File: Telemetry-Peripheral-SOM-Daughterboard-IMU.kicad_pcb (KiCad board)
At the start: 2 copper layers, 39 x 54 mm, 34 parts, among them IC1 FS3000-1015, J1 Conn_02x10_Odd_Even, J2 Conn_01x03_Pin, J3 Conn_01x03_Pin, J4 Conn_01x03_Pin, U1 LSM6DSV

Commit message: changes to I2C
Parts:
- renumbered Temp1 to TP1, Temp2 to TP2, Temp3 to TP3, Airflow_SDA to TP4, Airflow_SCL to TP5
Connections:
- IC1 pad 6: /I2C2_SDA -> /I2C1_SDA
- IC1 pad 7: /I2C2_SCL -> /I2C1_SCL
- TP4 pad 1: /I2C2_SDA -> /I2C1_SDA
- TP5 pad 1: /I2C2_SCL -> /I2C1_SCL
- U1 pad 4: /I2C1_SDA -> /I2C2_SDA
- U1 pad 9: /I2C1_SCL -> /I2C2_SCL
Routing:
- net /I2C2_SCL: track 43.3 -> 18.5 mm, vias 3 -> 0
- net /I2C1_SCL: track 17.5 -> 41.6 mm, vias 2 -> 1
- net /I2C2_SDA: track 44.4 -> 22.3 mm, vias 3 -> 2
- net /I2C1_SDA: track 22.7 -> 38.2 mm

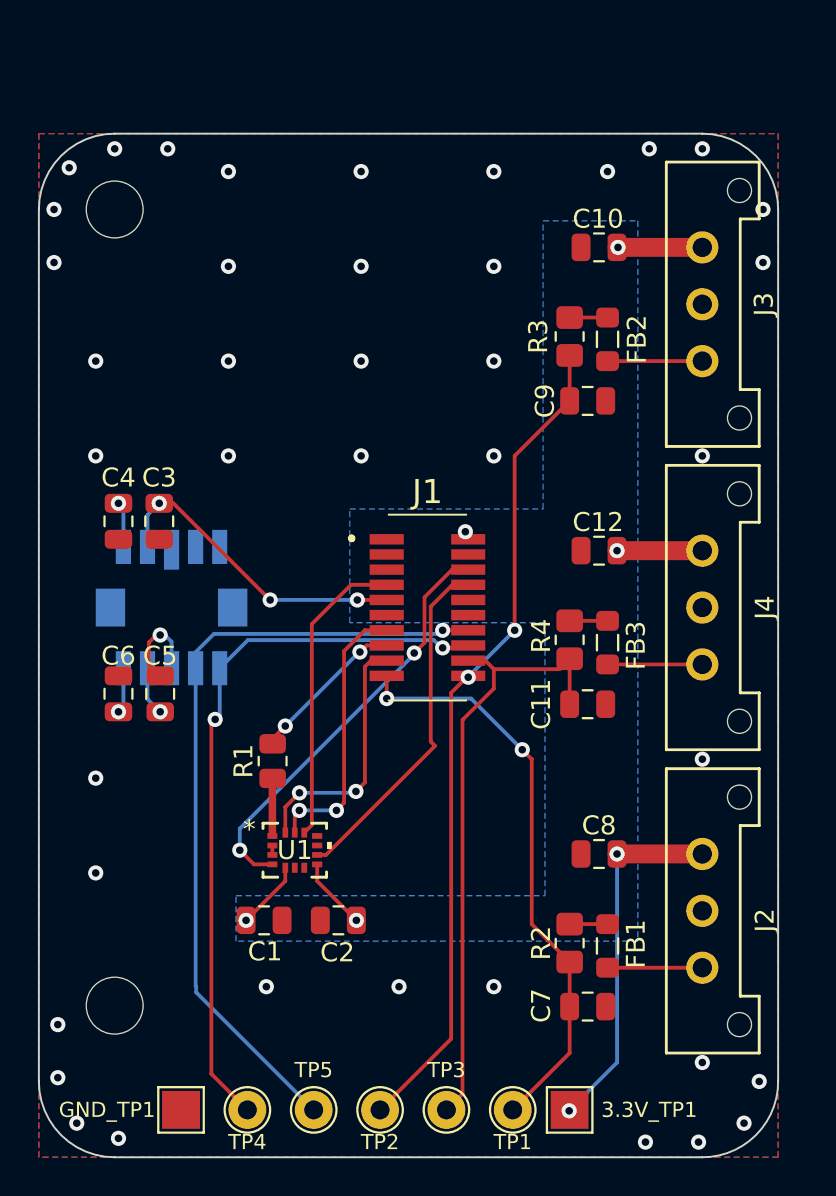
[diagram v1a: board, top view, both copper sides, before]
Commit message: moved testPoints to top of board
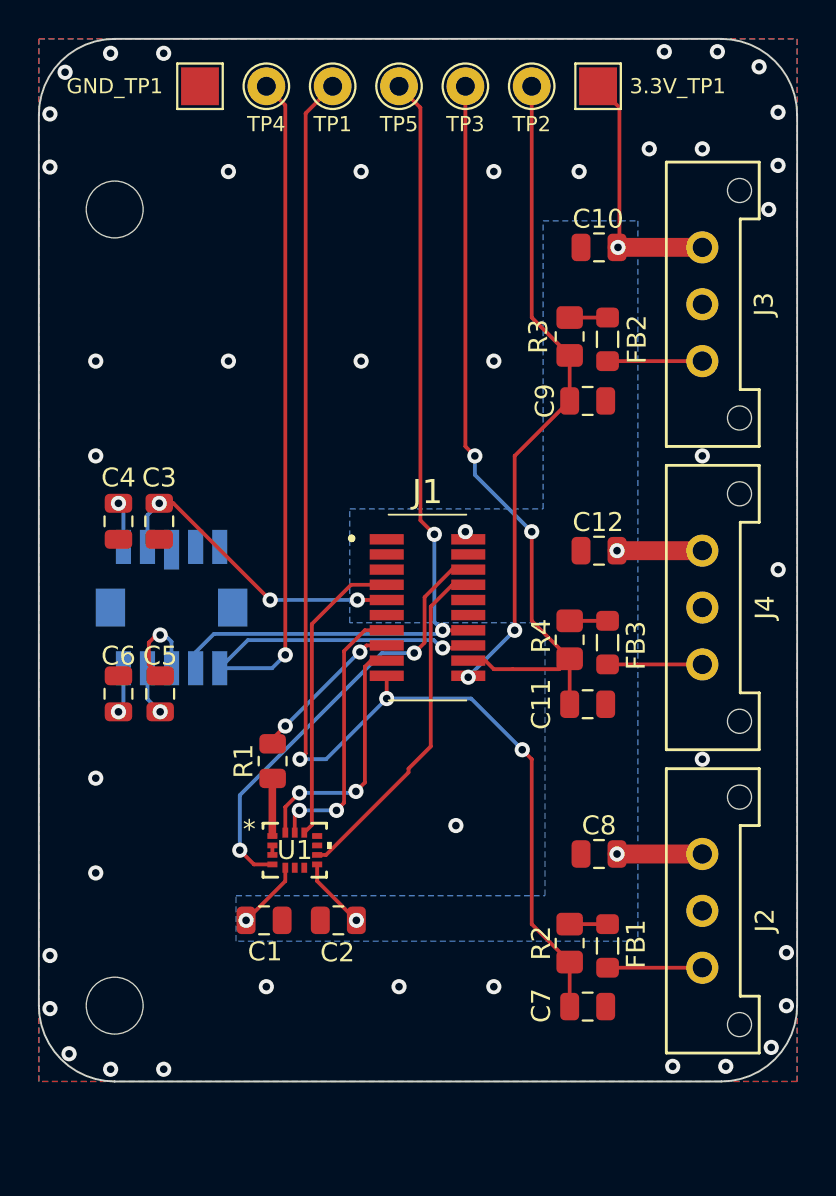
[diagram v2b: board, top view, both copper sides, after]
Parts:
- moved TP1 54.8 mm to (161.5, 63.5)
- moved TP2 54.6 mm to (172.0, 63.5)
- moved TP5 54.2 mm to (165.0, 63.5)
- moved 3.3V_TP1 54.0 mm to (175.5, 63.5)
- moved GND_TP1 54.0 mm to (154.5, 63.5)
- moved TP3 54.0 mm to (168.5, 63.5)
- moved TP4 54.0 mm to (158.0, 63.5)
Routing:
- net /SPI1_NSS: track 30.7 -> 66.2 mm, vias 2 -> 3
- net /I2C1_SDA: track 38.2 -> 48.1 mm
- net /PA1: track 44.0 -> 34.2 mm
- net /PA2: track 32.4 -> 40.6 mm, vias 0 -> 2
- net +3.3V: track 52.8 -> 47.1 mm, vias 10 -> 9
- net /I2C1_SCL: track 41.6 -> 45.4 mm, vias 1 -> 2
- net /I2C2_SDA: track 22.3 -> 23.4 mm
- net GND: vias 40 -> 41
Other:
- board size 39 x 54 mm -> 40 x 55 mm

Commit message: changes to silkscreen naming
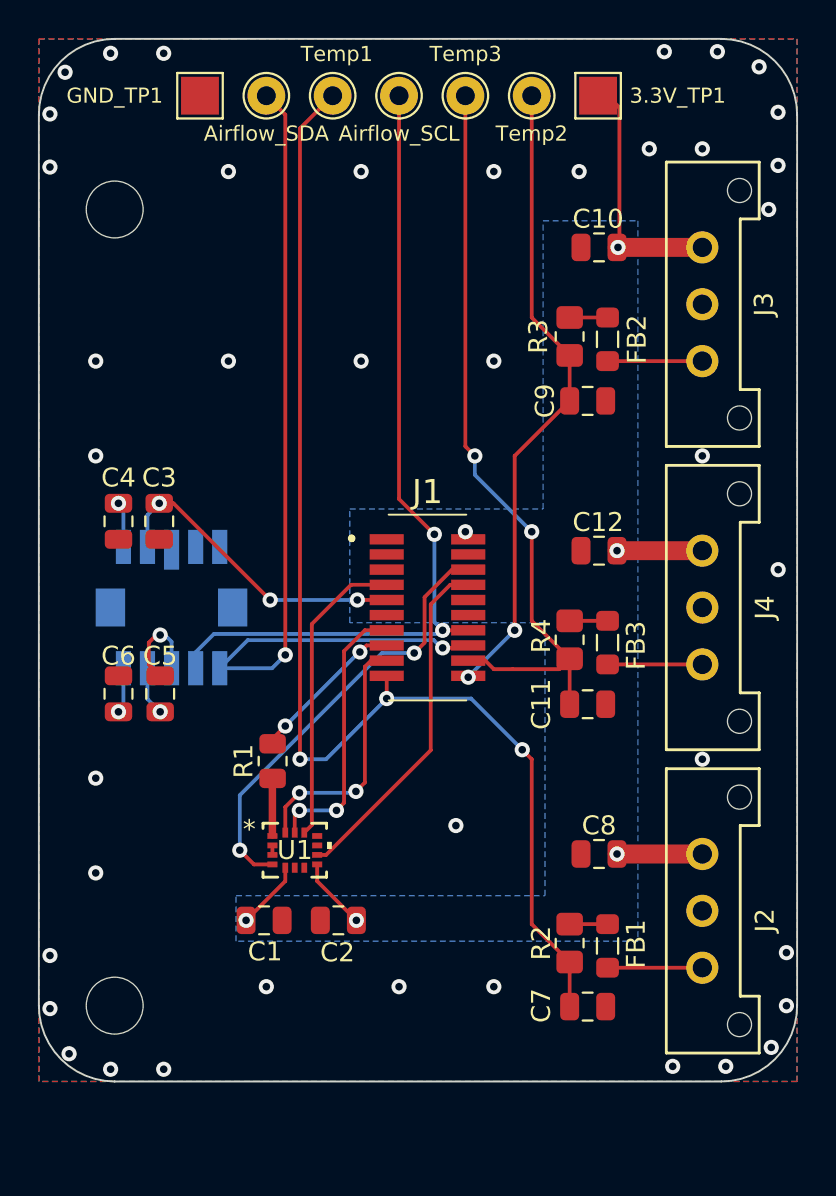
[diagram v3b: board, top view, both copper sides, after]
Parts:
- moved 3.3V_TP1 0.50 mm to (175.5, 64.0)
- moved Airflow_SCL 0.50 mm to (165.0, 64.0)
- moved Airflow_SDA 0.50 mm to (158.0, 64.0)
- moved GND_TP1 0.50 mm to (154.5, 64.0)
- moved Temp1 0.50 mm to (161.5, 64.0)
- moved Temp2 0.50 mm to (172.0, 64.0)
- moved Temp3 0.50 mm to (168.5, 64.0)
- renumbered TP5 to Airflow_SCL, TP4 to Airflow_SDA, TP1 to Temp1, TP2 to Temp2, TP3 to Temp3
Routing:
- net /SPI1_NSS: track 66.2 -> 65.7 mm
- net /PA2: track 40.6 -> 40.1 mm
- net /PA1: track 34.2 -> 33.7 mm
- net /I2C1_SDA: track 48.1 -> 47.6 mm
- net /I2C1_SCL: track 45.4 -> 44.9 mm
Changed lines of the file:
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@@
   )
   (footprint "TestPoint:TestPoint_THTPad_D2.0mm_Drill1.0mm" (layer "F.Cu")
-    (at 158 63.5)
+    (at 158 64)
     (descr "THT pad as test Point, diameter 2.0mm, hole diameter 1.0mm")
     (tags "test point THT pad")
@@
     (property "ki_keywords" "test point tp")
     (attr exclude_from_pos_files)
-    (fp_text reference "TP4" (at 0 2) (layer "F.SilkS")
+    (fp_text reference "Airflow_SDA" (at 0 2) (layer "F.SilkS")
         (effects (font (size 0.8 0.8) (thickness 0.15)))
     )
@@
   )
   (footprint "TestPoint:TestPoint_THTPad_D2.0mm_Drill1.0mm" (layer "F.Cu")
-    (at 161.5 63.5)
+    (at 161.5 64)
     (descr "THT pad as test Point, diameter 2.0mm, hole diameter 1.0mm")
     (tags "test point THT pad")
@@
     (property "ki_keywords" "test point tp")
     (attr exclude_from_pos_files)
-    (fp_text reference "TP1" (at 0 2) (layer "F.SilkS")
+    (fp_text reference "Temp1" (at 0.214262 -2.2) (layer "F.SilkS")
         (effects (font (size 0.8 0.8) (thickness 0.15)))
     )
@@
   )
   (footprint "TestPoint:TestPoint_THTPad_D2.0mm_Drill1.0mm" (layer "F.Cu")
-    (at 168.5 63.5)
+    (at 168.5 64)
     (descr "THT pad as test Point, diameter 2.0mm, hole diameter 1.0mm")
     (tags "test point THT pad")
@@
     (property "ki_keywords" "test point tp")
     (attr exclude_from_pos_files)
-    (fp_text reference "TP3" (at 0 2) (layer "F.SilkS")
+    (fp_text reference "Temp3" (at 0.011904 -2.2) (layer "F.SilkS")
         (effects (font (size 0.8 0.8) (thickness 0.15)))
     )
@@
   )
   (footprint "TestPoint:TestPoint_Pad_2.0x2.0mm" (layer "F.Cu")
-    (at 175.5 63.5)
+    (at 175.5 64)
     (descr "SMD rectangular pad as test Point, square 2.0mm side length")
     (tags "test point SMD pad rectangle square")
@@
   )
   (footprint "TestPoint:TestPoint_THTPad_D2.0mm_Drill1.0mm" (layer "F.Cu")
-    (at 165 63.5)
+    (at 165 64)
     (descr "THT pad as test Point, diameter 2.0mm, hole diameter 1.0mm")
     (tags "test point THT pad")
@@
     (property "ki_keywords" "test point tp")
     (attr exclude_from_pos_files)
-    (fp_text reference "TP5" (at 0 2) (layer "F.SilkS")
+    (fp_text reference "Airflow_SCL" (at 0 2) (layer "F.SilkS")
         (effects (font (size 0.8 0.8) (thickness 0.15)))
     )
@@
   )
   (footprint "TestPoint:TestPoint_Pad_2.0x2.0mm" (layer "F.Cu")
-    (at 154.5 63.5)
+    (at 154.5 64)
     (descr "SMD rectangular pad as test Point, square 2.0mm side length")
     (tags "test point SMD pad rectangle square")
@@
   )
   (footprint "TestPoint:TestPoint_THTPad_D2.0mm_Drill1.0mm" (layer "F.Cu")
-    (at 172 63.5)
+    (at 172 64)
     (descr "THT pad as test Point, diameter 2.0mm, hole diameter 1.0mm")
     (tags "test point THT pad")
@@
     (property "ki_keywords" "test point tp")
     (attr exclude_from_pos_files)
-    (fp_text reference "TP2" (at 0 2) (layer "F.SilkS")
+    (fp_text reference "Temp2" (at 0 2) (layer "F.SilkS")
         (effects (font (size 0.8 0.8) (thickness 0.15)))
     )
@@
   (segment (start 162.468629 89.8) (end 160.4 91.868629) (width 0.2) (layer "F.Cu") (net 7))
   (segment (start 164.35 89.8) (end 162.468629 89.8) (width 0.2) (layer "F.Cu") (net 7))
-  (segment (start 165.5 99.5) (end 166.673 98.327) (width 0.2) (layer "F.Cu") (net 8))
-  (segment (start 166.673 90.948) (end 167.821 89.8) (width 0.2) (layer "F.Cu") (net 8))
-  (segment (start 165.5 99.6975) (end 165.5 99.5) (width 0.2) (layer "F.Cu") (net 8))
-  (segment (start 161.147801 104.049699) (end 165.5 99.6975) (width 0.2) (layer "F.Cu") (net 8))
   (segment (start 160.681101 104.049699) (end 161.147801 104.049699) (width 0.2) (layer "F.Cu") (net 8))
-  (segment (start 167.821 89.8) (end 168.65 89.8) (width 0.2) (layer "F.Cu") (net 8))
-  (segment (start 166.673 98.327) (end 166.673 90.948) (width 0.2) (layer "F.Cu") (net 8))
+  (segment (start 167.7 89.8) (end 168.65 89.8) (width 0.2) (layer "F.Cu") (net 8))
+  (segment (start 161.147801 104.049699) (end 166.673 98.5245) (width 0.2) (layer "F.Cu") (net 8))
+  (segment (start 166.673 98.5245) (end 166.673 90.827) (width 0.2) (layer "F.Cu") (net 8))
+  (segment (start 166.673 90.827) (end 167.7 89.8) (width 0.2) (layer "F.Cu") (net 8))
   (segment (start 161.7 101.7) (end 162.1 101.3) (width 0.2) (layer "F.Cu") (net 11))
   (segment (start 159.739515 101.701471) (end 159.500001 101.940985) (width 0.2) (layer "F.Cu") (net 11))
@@
   (segment (start 161.7 101.7) (end 159.740986 101.7) (width 0.2) (layer "B.Cu") (net 11))
   (segment (start 159.740986 101.7) (end 159.739515 101.701471) (width 0.2) (layer "B.Cu") (net 11))
-  (segment (start 165 63.5) (end 166.127 64.627) (width 0.2) (layer "F.Cu") (net 12))
-  (segment (start 166.127 86.399718) (end 166.863641 87.136359) (width 0.2) (layer "F.Cu") (net 12))
+  (segment (start 165 64) (end 165 85.272718) (width 0.2) (layer "F.Cu") (net 12))
+  (segment (start 165 85.272718) (end 166.863641 87.136359) (width 0.2) (layer "F.Cu") (net 12))
   (segment (start 167.3 92.2) (end 168.65 92.2) (width 0.2) (layer "F.Cu") (net 12))
-  (segment (start 166.127 64.627) (end 166.127 86.399718) (width 0.2) (layer "F.Cu") (net 12))
   (via (at 167.3 92.2) (size 0.8) (drill 0.4) (layers "F.Cu" "B.Cu") (net 12))
   (via (at 166.863641 87.136359) (size 0.8) (drill 0.4) (layers "F.Cu" "B.Cu") (net 12))
@@
   (segment (start 162.904311 93.345689) (end 162.93646 93.345689) (width 0.2) (layer "B.Cu") (net 13))
   (segment (start 159 97.25) (end 162.904311 93.345689) (width 0.2) (layer "B.Cu") (net 13))
-  (segment (start 159 93.5) (end 159 64.5) (width 0.2) (layer "F.Cu") (net 14))
-  (segment (start 159 64.5) (end 158 63.5) (width 0.2) (layer "F.Cu") (net 14))
+  (segment (start 159 65) (end 159 93.5) (width 0.2) (layer "F.Cu") (net 14))
   (segment (start 167.3 93.126503) (end 168.523497 93.126503) (width 0.2) (layer "F.Cu") (net 14))
   (segment (start 168.523497 93.126503) (end 168.65 93) (width 0.2) (layer "F.Cu") (net 14))
+  (segment (start 158 64) (end 159 65) (width 0.2) (layer "F.Cu") (net 14))
   (via (at 167.3 93.126503) (size 0.8) (drill 0.4) (layers "F.Cu" "B.Cu") (net 14))
   (via (at 159 93.5) (size 0.8) (drill 0.4) (layers "F.Cu" "B.Cu") (net 14))
@@
   (segment (start 162.651499 100.775001) (end 162.7265 100.7) (width 0.2) (layer "B.Cu") (net 15))
   (segment (start 174 109.7) (end 174 112.05) (width 0.2) (layer "F.Cu") (net 16))
-  (segment (start 160.073 64.927) (end 160.073 98.7005) (width 0.2) (layer "F.Cu") (net 16))
+  (segment (start 161.5 64) (end 159.7735 65.7265) (width 0.2) (layer "F.Cu") (net 16))
   (segment (start 172 107.7) (end 174 109.7) (width 0.2) (layer "F.Cu") (net 16))
   (segment (start 164.35 95.8) (end 164.35 94.6) (width 0.2) (layer "F.Cu") (net 16))
-  (segment (start 161.5 63.5) (end 160.073 64.927) (width 0.2) (layer "F.Cu") (net 16))
   (segment (start 171.5 98.5) (end 172 99) (width 0.2) (layer "F.Cu") (net 16))
-  (segment (start 160.073 98.7005) (end 159.7735 99) (width 0.2) (layer "F.Cu") (net 16))
+  (segment (start 159.7735 65.7265) (end 159.7735 99) (width 0.2) (layer "F.Cu") (net 16))
   (segment (start 172 99) (end 172 107.7) (width 0.2) (layer "F.Cu") (net 16))
   (via (at 159.7735 99) (size 0.8) (drill 0.4) (layers "F.Cu" "B.Cu") (net 16))
@@
   (segment (start 153 92.8) (end 153 94.2) (width 0.2) (layer "B.Cu") (net 27))
   (segment (start 152.4 92.45) (end 152.65 92.45) (width 0.2) (layer "B.Cu") (net 27))
+  (segment (start 172 64) (end 172 75.7) (width 0.2) (layer "F.Cu") (net 28))
   (segment (start 172 75.7) (end 174 77.7) (width 0.2) (layer "F.Cu") (net 28))
   (segment (start 171.1 92.2) (end 171.1 83) (width 0.2) (layer "F.Cu") (net 28))
   (segment (start 171.1 83) (end 174 80.1) (width 0.2) (layer "F.Cu") (net 28))
   (segment (start 174 77.7) (end 174 80.1) (width 0.2) (layer "F.Cu") (net 28))
-  (segment (start 172 63.5) (end 172 75.7) (width 0.2) (layer "F.Cu") (net 28))
   (via (at 171.1 92.2) (size 0.8) (drill 0.4) (layers "F.Cu" "B.Cu") (net 28))
   (via (at 168.65 94.674502) (size 0.8) (drill 0.4) (layers "F.Cu" "B.Cu") (net 28))
@@
   (segment (start 168.65 94.65) (end 171.1 92.2) (width 0.2) (layer "B.Cu") (net 28))
   (segment (start 169.55 93.8) (end 170 94.25) (width 0.2) (layer "F.Cu") (net 29))
-  (segment (start 168.5 82.5) (end 168.5 63.5) (width 0.2) (layer "F.Cu") (net 29))
+  (segment (start 168.5 82.5) (end 169 83) (width 0.2) (layer "F.Cu") (net 29))
   (segment (start 172 91.7) (end 174 93.7) (width 0.2) (layer "F.Cu") (net 29))
   (segment (start 172 87) (end 172 91.7) (width 0.2) (layer "F.Cu") (net 29))
   (segment (start 168.65 93.8) (end 169.55 93.8) (width 0.2) (layer "F.Cu") (net 29))
   (segment (start 171 94.25) (end 173.45 94.25) (width 0.2) (layer "F.Cu") (net 29))
-  (segment (start 169 83) (end 168.5 82.5) (width 0.2) (layer "F.Cu") (net 29))
+  (segment (start 168.5 64) (end 168.5 82.5) (width 0.2) (layer "F.Cu") (net 29))
   (segment (start 173.45 94.25) (end 174 93.7) (width 0.2) (layer "F.Cu") (net 29))
   (segment (start 174 93.7) (end 174 96.1) (width 0.2) (layer "F.Cu") (net 29))

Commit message: spaced out filtering components
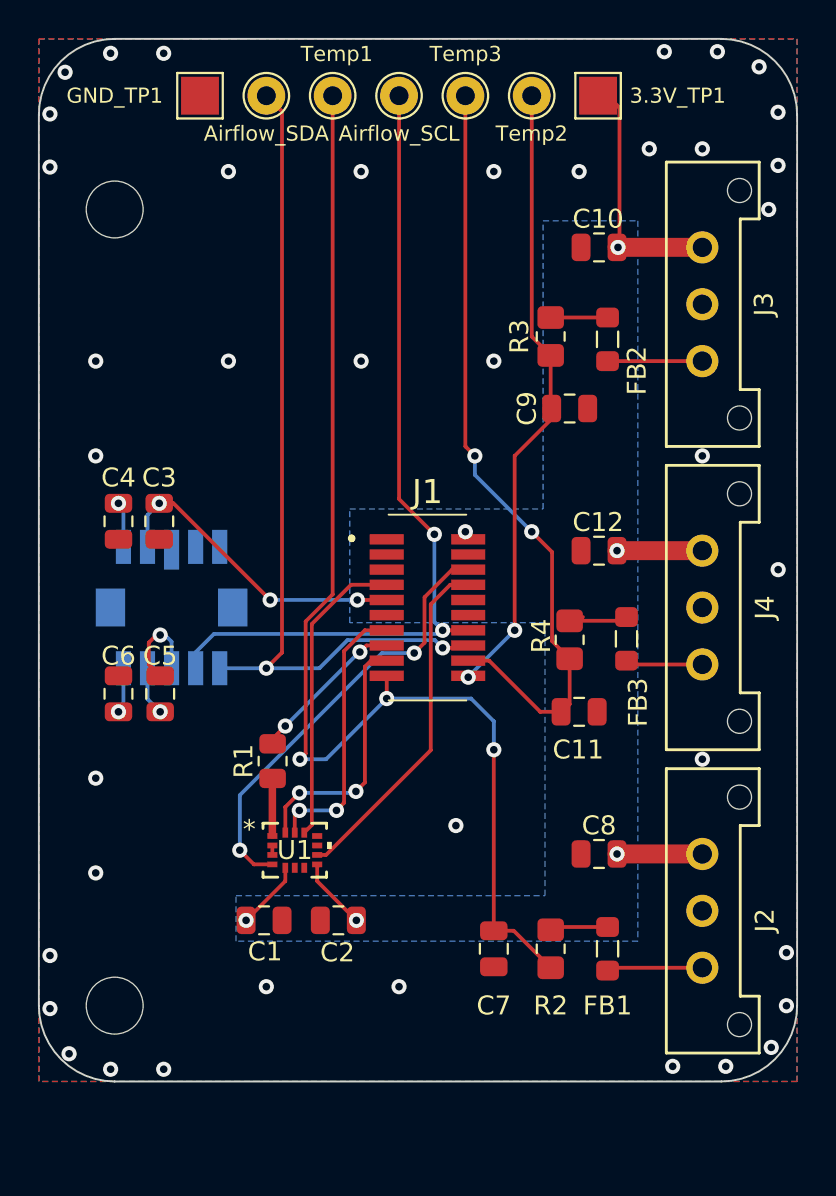
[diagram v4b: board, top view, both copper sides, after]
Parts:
- moved C7 5.81 mm to (170.0, 109.0), turned to -90 degrees
- moved R2 1.04 mm to (173.0, 109.0)
- moved C9 1.03 mm to (174.0, 80.5)
- moved FB3 1.02 mm to (177.0, 92.7)
- moved R3 1.00 mm to (173.0, 76.7)
- moved C11 0.60 mm to (174.5, 96.5)
- moved FB1 0.15 mm to (176.0, 109.0)
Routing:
- net /I2C1_SDA: track 47.6 -> 44.8 mm
- net /SPI1_NSS: track 65.7 -> 63.8 mm
- net Net-(FB1-Pad1): track 2.00 -> 3.49 mm
- net Net-(FB3-Pad1): track 2.00 -> 3.37 mm
- net Net-(FB2-Pad1): track 2.00 -> 3.00 mm
- net Net-(J4-Pin_3): track 5.00 -> 4.08 mm
- net /PA2: track 40.1 -> 41.0 mm
- net /PA1: track 33.7 -> 32.9 mm
- net GND: track 0.50 -> 0.57 mm, vias 41 -> 40
